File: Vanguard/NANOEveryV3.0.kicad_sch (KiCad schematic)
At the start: 57 parts, among them IC1 MPM3610, J1 -, J2 DNP, Q1 BSS138PS, Q2 BSS138PS, U1 ATMEGA4809, U2 AP2112K-3.3, U3 ATSAMD11D14A, U4 ICM-20602, U5 LM34DM_NOPB

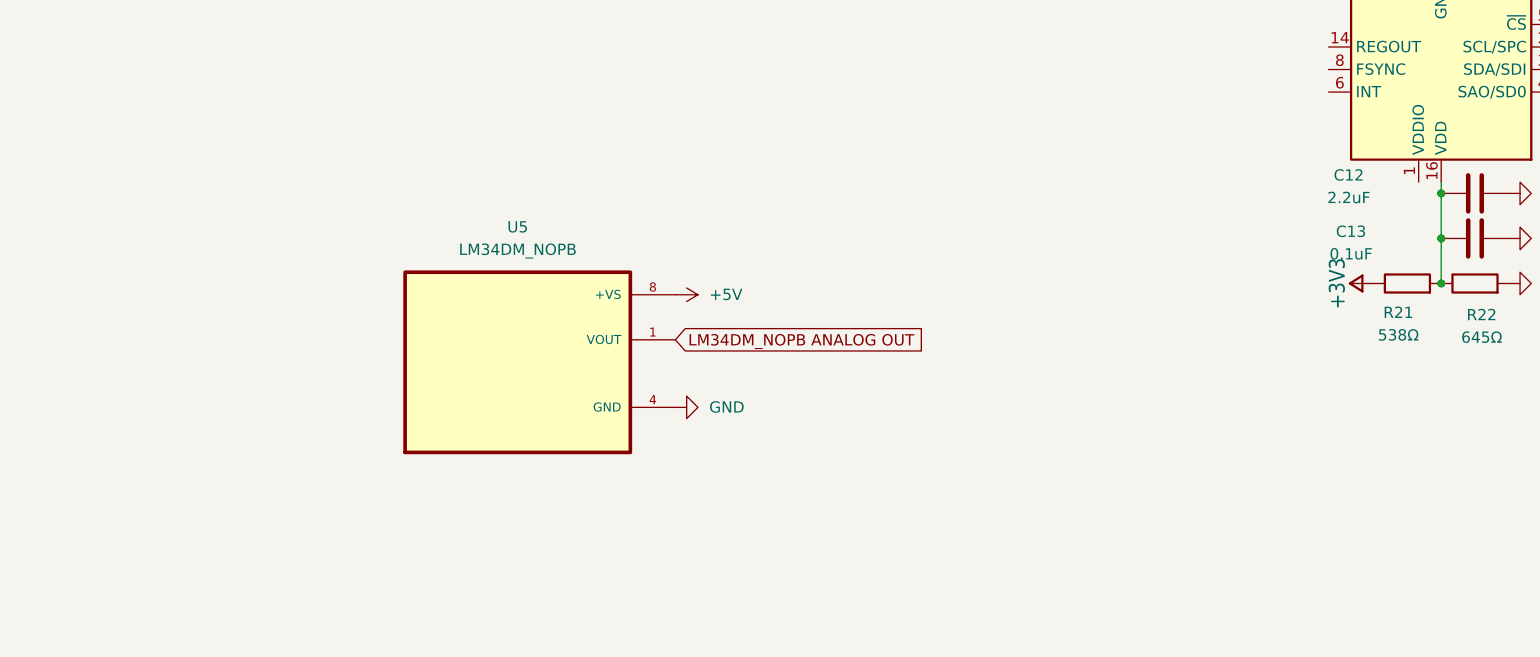
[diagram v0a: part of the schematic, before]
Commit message: Added 2 decoupling capacitors to the temp. sensor
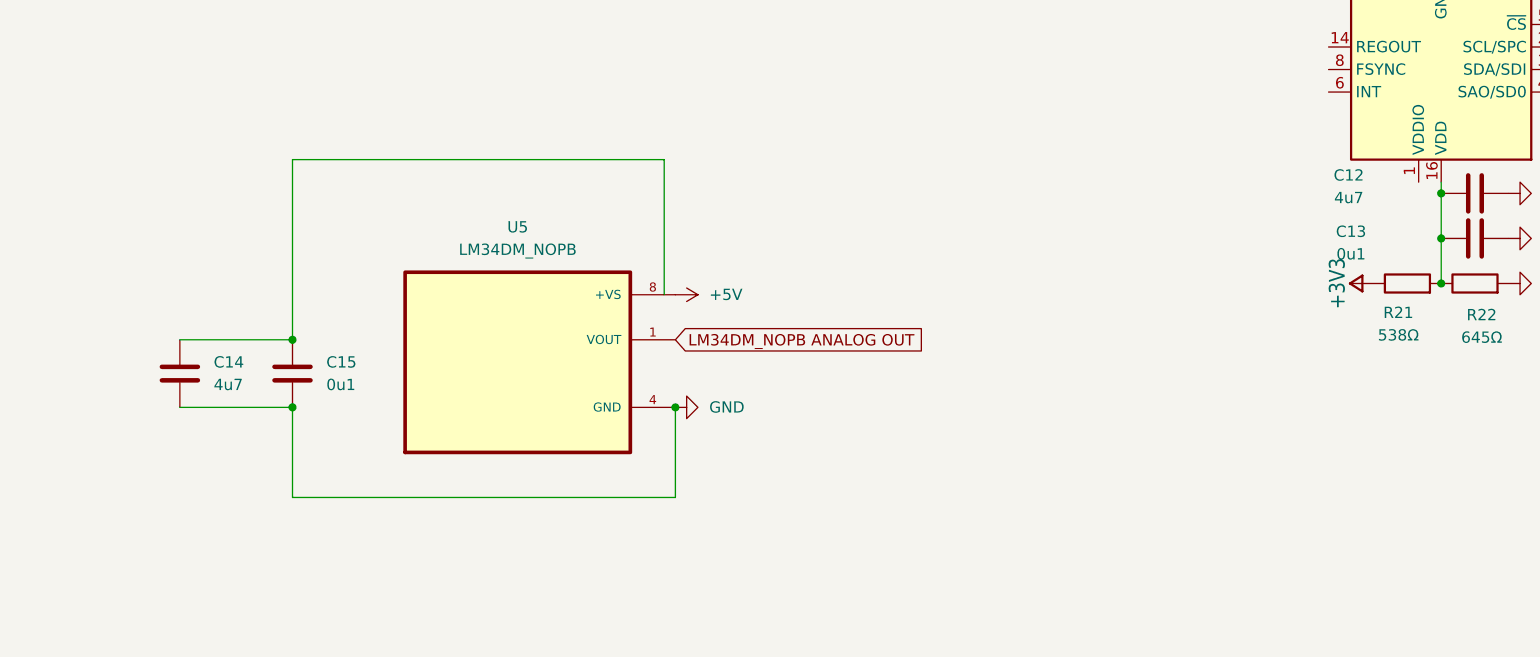
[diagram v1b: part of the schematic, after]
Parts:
- added C14: 4u7, symbol Device:C
- added C15: 0u1, symbol Device:C
- C12: value 2.2uF -> 4u7
- C13: value 0.1uF -> 0u1
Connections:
- net GND: now also C14.2, C15.2
- new net: C14.1, C15.1
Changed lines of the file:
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@@
 	)
 	(junction
+		(at 82.55 213.36)
+		(diameter 0)
+		(color 0 0 0 0)
+	)
+	(junction
 		(at 212.09 201.93)
 		(diameter 0)
@@
 	)
 	(junction
+		(at 125.73 220.98)
+		(diameter 0)
+		(color 0 0 0 0)
+	)
+	(junction
 		(at 59.69 152.4)
 		(diameter 0)
@@
 	)
 	(junction
+		(at 82.55 220.98)
+		(diameter 0)
+		(color 0 0 0 0)
+	)
+	(junction
 		(at 248.92 208.28)
 		(diameter 0)
@@
 	(wire
 		(pts
+			(xy 124.46 193.04) (xy 124.46 208.28)
+		)
+		(stroke
+			(width 0)
+			(type default)
+		)
+	)
+	(wire
+		(pts
 			(xy 375.92 186.69) (xy 353.06 186.69)
 		)
@@
 	(wire
 		(pts
+			(xy 125.73 220.98) (xy 125.73 231.14)
+		)
+		(stroke
+			(width 0)
+			(type default)
+		)
+	)
+	(wire
+		(pts
 			(xy 78.74 152.4) (xy 99.06 152.4)
 		)
@@
 	(wire
 		(pts
+			(xy 69.85 220.98) (xy 82.55 220.98)
+		)
+		(stroke
+			(width 0)
+			(type default)
+		)
+	)
+	(wire
+		(pts
 			(xy 149.86 33.02) (xy 149.86 36.83)
 		)
@@
 	(wire
 		(pts
+			(xy 82.55 231.14) (xy 125.73 231.14)
+		)
+		(stroke
+			(width 0)
+			(type default)
+		)
+	)
+	(wire
+		(pts
 			(xy 330.2 83.82) (xy 350.52 83.82)
 		)
@@
 	(wire
 		(pts
+			(xy 82.55 213.36) (xy 82.55 193.04)
+		)
+		(stroke
+			(width 0)
+			(type default)
+		)
+	)
+	(wire
+		(pts
 			(xy 184.15 123.19) (xy 186.69 123.19)
 		)
@@
 	(wire
 		(pts
+			(xy 82.55 220.98) (xy 82.55 231.14)
+		)
+		(stroke
+			(width 0)
+			(type default)
+		)
+	)
+	(wire
+		(pts
 			(xy 180.34 107.95) (xy 187.96 107.95)
 		)
@@
 	(wire
 		(pts
+			(xy 69.85 213.36) (xy 82.55 213.36)
+		)
+		(stroke
+			(width 0)
+			(type default)
+		)
+	)
+	(wire
+		(pts
 			(xy 63.5 152.4) (xy 59.69 152.4)
 		)
@@
 		)
 	)
+	(wire
+		(pts
+			(xy 82.55 193.04) (xy 124.46 193.04)
+		)
+		(stroke
+			(width 0)
+			(type default)
+		)
+	)
 	(bus
 		(pts
@@
 			)
 		)
-		(property "Value" "2.2uF"
+		(property "Value" "4u7"
 			(at 201.676 197.358 90)
 			(effects
@@
 	)
 	(symbol
+		(lib_id "Device:C")
+		(at 82.55 217.17 0)
+		(unit 1)
+		(exclude_from_sim no)
+		(in_bom yes)
+		(on_board yes)
+		(dnp no)
+		(fields_autoplaced yes)
+		(property "Reference" "C15"
+			(at 86.36 215.8999 0)
+			(effects
+				(font
+					(size 1.27 1.27)
+				)
+				(justify left)
+			)
+		)
+		(property "Value" "0u1"
+			(at 86.36 218.4399 0)
+			(effects
+				(font
+					(size 1.27 1.27)
+				)
+				(justify left)
+			)
+		)
+		(property "Footprint" ""
+			(at 83.5152 220.98 0)
+			(effects
+				(font
+					(size 1.27 1.27)
+				)
+				(hide yes)
+			)
+		)
+		(property "Datasheet" "~"
+			(at 82.55 217.17 0)
+			(effects
+				(font
+					(size 1.27 1.27)
+				)
+				(hide yes)
+			)
+		)
+		(property "Description" "Unpolarized capacitor"
+			(at 82.55 217.17 0)
+			(effects
+				(font
+					(size 1.27 1.27)
+				)
+				(hide yes)
+			)
+		)
+		(pin "2"
+		)
+		(pin "1"
+		)
+		(instances
+			(project ""
+				(path "/34ea8acc-c59c-4b5c-bba1-2d3f07551c63"
+					(reference "C15")
+					(unit 1)
+				)
+			)
+		)
+	)
+	(symbol
 		(lib_id "power:GND")
 		(at 219.71 196.85 90)
@@
 			)
 		)
-		(property "Value" "0.1uF"
+		(property "Value" "0u1"
 			(at 201.93 203.708 90)
 			(effects
@@
 					(unit 1)
 				)
+			)
+		)
+	)
+	(symbol
+		(lib_id "Device:C")
+		(at 69.85 217.17 0)
+		(unit 1)
+		(exclude_from_sim no)
+		(in_bom yes)
+		(on_board yes)
+		(dnp no)
+		(fields_autoplaced yes)
+		(property "Reference" "C14"
+			(at 73.66 215.8999 0)
+			(effects
+				(font
+					(size 1.27 1.27)
+				)
+				(justify left)
+			)
+		)
+		(property "Value" "4u7"
+			(at 73.66 218.4399 0)
+			(effects
+				(font
+					(size 1.27 1.27)
+				)
+				(justify left)
+			)
+		)
+		(property "Footprint" ""
+			(at 70.8152 220.98 0)
+			(effects
+				(font
+					(size 1.27 1.27)
+				)
+				(hide yes)
+			)
+		)
+		(property "Datasheet" "~"
+			(at 69.85 217.17 0)
+			(effects
+				(font
+					(size 1.27 1.27)
+				)
+				(hide yes)
+			)
+		)
+		(property "Description" "Unpolarized capacitor"
+			(at 69.85 217.17 0)
+			(effects
+				(font
+					(size 1.27 1.27)
+				)
+				(hide yes)
+			)
+		)
+		(pin "2"
+		)
+		(pin "1"
+		)
+		(instances
+			(project ""
+				(path "/34ea8acc-c59c-4b5c-bba1-2d3f07551c63"
+					(reference "C14")
+					(unit 1)
+				)

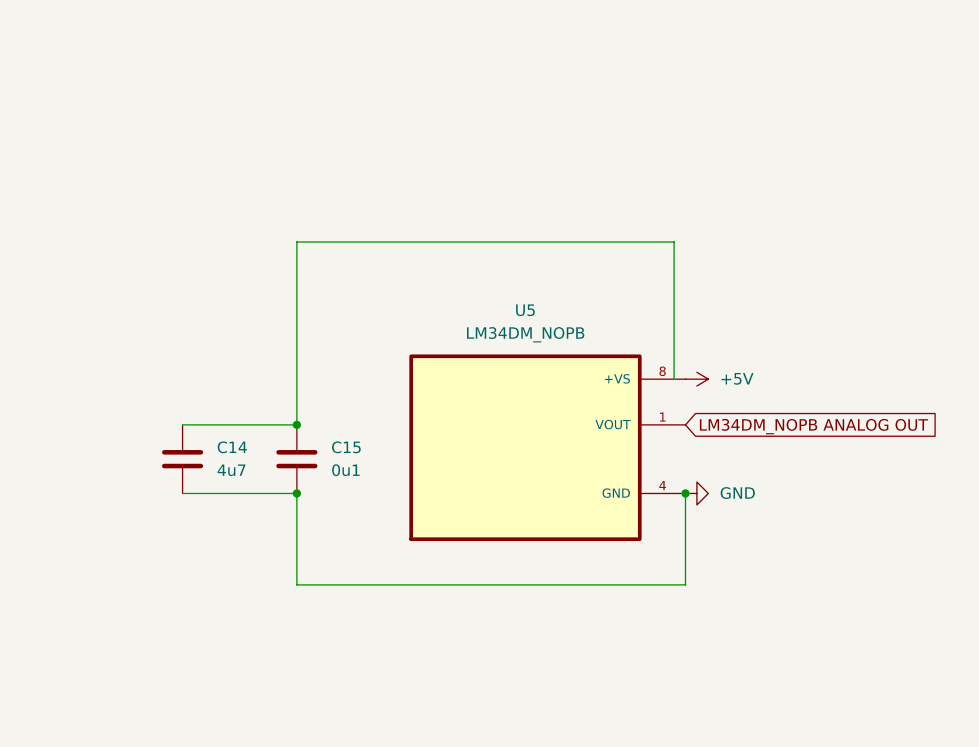
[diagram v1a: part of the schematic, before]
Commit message: slight changes in the capacitor arrangement
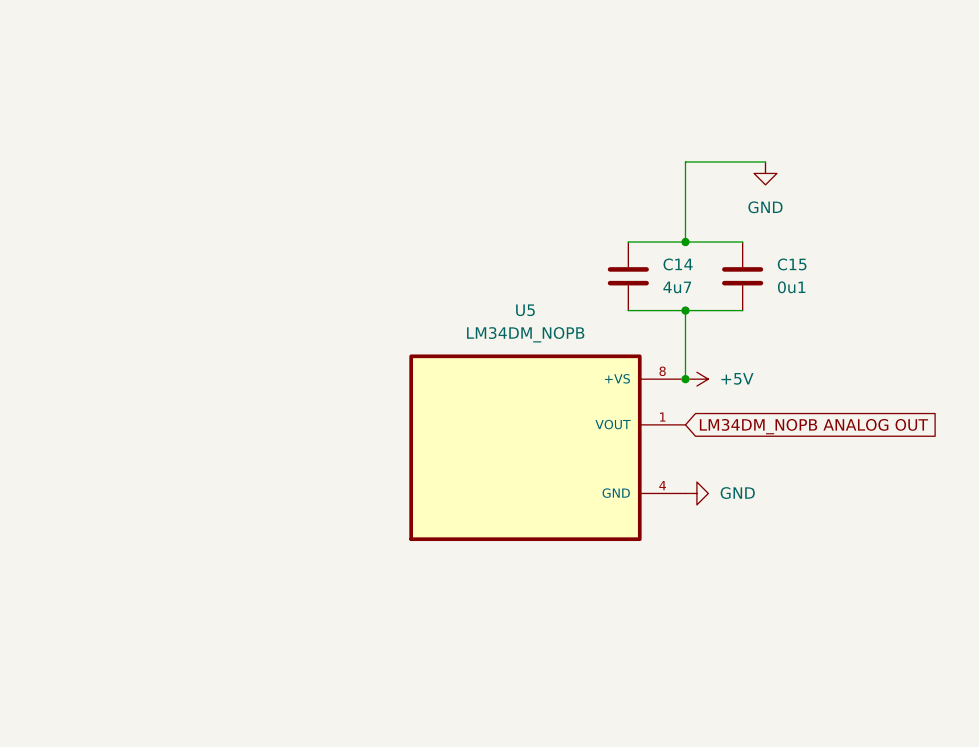
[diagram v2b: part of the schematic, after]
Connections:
- net +5V: now also C14.2, C15.2
- net GND: now also C14.1, C15.1; no longer C14.2, C15.2

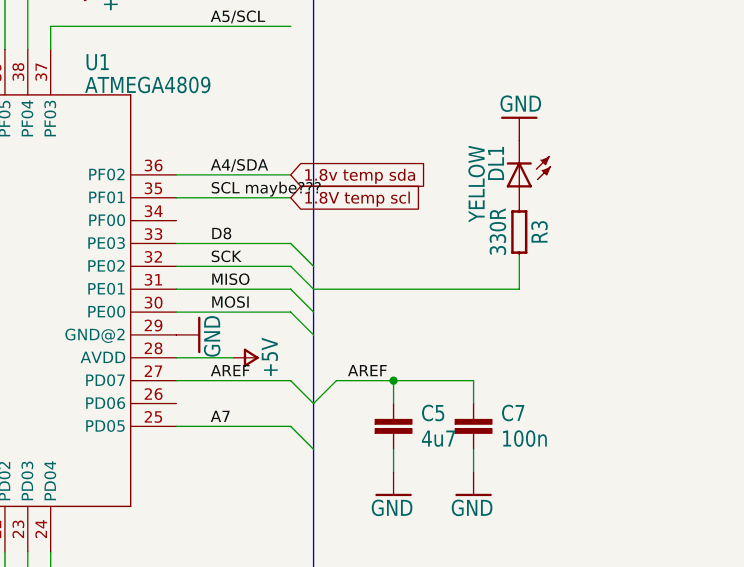
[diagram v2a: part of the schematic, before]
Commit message: finished layout except sd card
lots of discontinuities need to be fixed
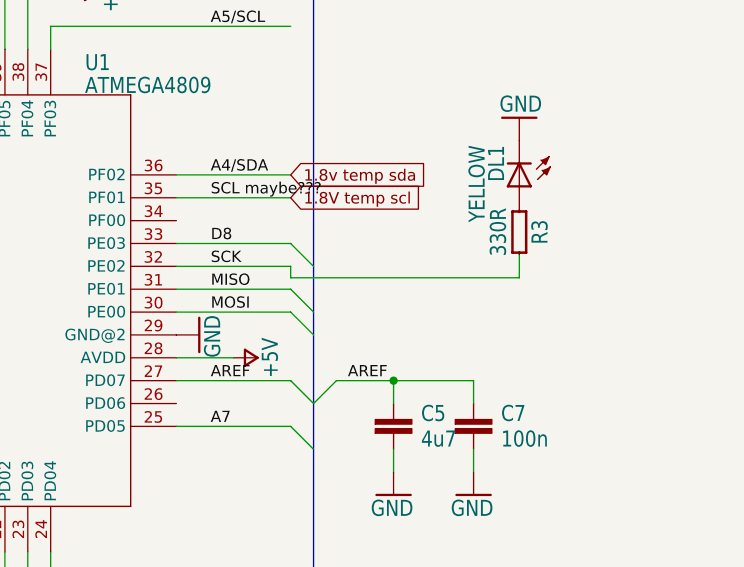
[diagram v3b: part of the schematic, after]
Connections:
- net SCK: now also R3.2
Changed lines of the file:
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@@
 	)
 	(bus_entry
-		(at 350.52 184.15)
-		(size 2.54 2.54)
-		(stroke
-			(width 0)
-			(type default)
-		)
-	)
-	(bus_entry
 		(at 350.52 88.9)
 		(size 2.54 2.54)
@@
 		)
 	)
-	(wire
-		(pts
-			(xy 375.92 186.69) (xy 353.06 186.69)
-		)
-		(stroke
-			(width 0)
-			(type default)
-		)
-	)
 	(bus
 		(pts
@@
 	(wire
 		(pts
+			(xy 350.52 184.15) (xy 350.52 185.42)
+		)
+		(stroke
+			(width 0.1524)
+			(type solid)
+		)
+	)
+	(wire
+		(pts
 			(xy 248.92 208.28) (xy 264.16 208.28)
 		)
@@
 	(wire
 		(pts
-			(xy 375.92 182.88) (xy 375.92 186.69)
+			(xy 375.92 182.88) (xy 375.92 185.42)
 		)
 		(stroke
@@
 	(bus
 		(pts
-			(xy 353.06 186.69) (xy 353.06 184.15)
+			(xy 353.06 184.15) (xy 353.06 189.23)
 		)
 		(stroke
@@
 	(wire
 		(pts
+			(xy 350.52 185.42) (xy 375.92 185.42)
+		)
+		(stroke
+			(width 0.1524)
+			(type solid)
+		)
+	)
+	(wire
+		(pts
 			(xy 87.63 50.8) (xy 90.17 50.8)
 		)
@@
 		)
 	)
-	(bus
-		(pts
-			(xy 353.06 189.23) (xy 353.06 186.69)
-		)
-		(stroke
-			(width 0.762)
-			(type solid)
-		)
-	)
 	(wire
 		(pts
@@
 	)
 	(symbol
+		(lib_id "NANOEveryV3.0-eagle-import:+3V3")
+		(at 149.86 27.94 0)
+		(unit 1)
+		(exclude_from_sim no)
+		(in_bom yes)
+		(on_board yes)
+		(dnp no)
+		(property "Reference" "#+3V04"
+			(at 149.86 27.94 0)
+			(effects
+				(font
+					(size 1.27 1.27)
+				)
+				(hide yes)
+			)
+		)
+		(property "Value" "+3V3"
+			(at 149.86 27.432 0)
+			(effects
+				(font
+					(size 1.778 1.5113)
+				)
+				(justify bottom)
+			)
+		)
+		(property "Footprint" ""
+			(at 149.86 27.94 0)
+			(effects
+				(font
+					(size 1.27 1.27)
+				)
+				(hide yes)
+			)
+		)
+		(property "Datasheet" ""
+			(at 149.86 27.94 0)
+			(effects
+				(font
+					(size 1.27 1.27)
+				)
+				(hide yes)
+			)
+		)
+		(property "Description" ""
+			(at 149.86 27.94 0)
+			(effects
+				(font
+					(size 1.27 1.27)
+				)
+				(hide yes)
+			)
+		)
+		(pin "1"
+		)
+		(instances
+			(project "NANOEveryV3.0"
+				(path "/34ea8acc-c59c-4b5c-bba1-2d3f07551c63"
+					(reference "#+3V04")
+					(unit 1)
+				)
+			)
+		)
+	)
+	(symbol
 		(lib_id "NANOEveryV3.0-eagle-import:R-0402")
 		(at 187.96 97.79 90)
@@
 					(unit 1)
 				)
-			)
-		)
-	)
-	(symbol
-		(lib_id "NANOEveryV3.0-eagle-import:+3V3")
-		(at 149.86 27.94 0)
-		(unit 1)
-		(exclude_from_sim no)
-		(in_bom yes)
-		(on_board yes)
-		(dnp no)
-		(property "Reference" "#+3V04"
-			(at 149.86 27.94 0)
-			(effects
-				(font
-					(size 1.27 1.27)
-				)
-				(hide yes)
-			)
-		)
-		(property "Value" "+3V3"
-			(at 149.86 27.432 0)
-			(effects
-				(font
-					(size 1.778 1.5113)
-				)
-				(justify bottom)
-			)
-		)
-		(property "Footprint" ""
-			(at 149.86 27.94 0)
-			(effects
-				(font
-					(size 1.27 1.27)
-				)
-				(hide yes)
-			)
-		)
-		(property "Datasheet" ""
-			(at 149.86 27.94 0)
-			(effects
-				(font
-					(size 1.27 1.27)
-				)
-				(hide yes)
-			)
-		)
-		(property "Description" ""
-			(at 149.86 27.94 0)
-			(effects
-				(font
-					(size 1.27 1.27)
-				)
-				(hide yes)
-			)
-		)
-		(pin "1"
-		)
-		(instances
-			(project ""
-				(path "/34ea8acc-c59c-4b5c-bba1-2d3f07551c63"
-					(reference "#+3V04")
-					(unit 1)
-				)

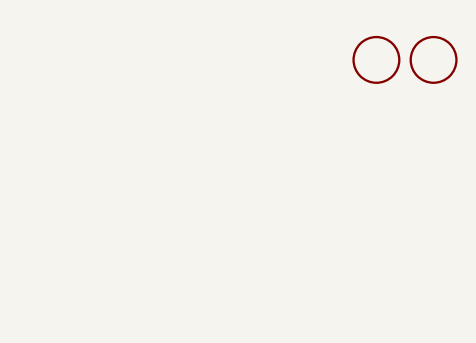
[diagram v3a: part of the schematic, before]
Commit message: added 2 footprints
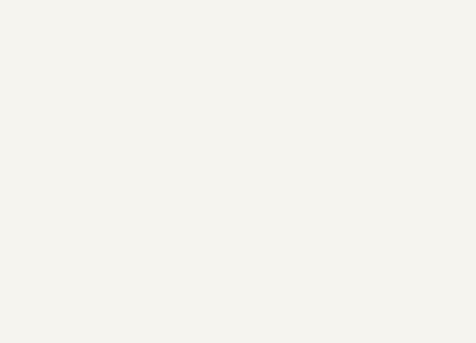
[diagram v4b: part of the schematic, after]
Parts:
- removed FD1, FD2: DNP, TestPoint:TestPoint_THTPad_1.0x1.0mm_Drill0.5mm, symbol NANOEveryV3.0-eagle-import:FIDUCIAL-1.5MM
- C14, C15: footprint (none) -> Capacitor_SMD:C_0402_1005Metric
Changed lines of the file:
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@@
 	)
 	(symbol
-		(lib_id "NANOEveryV3.0-eagle-import:FIDUCIAL-1.5MM")
-		(at 396.24 27.94 0)
-		(unit 1)
-		(exclude_from_sim no)
-		(in_bom yes)
-		(on_board yes)
-		(dnp no)
-		(property "Reference" "FD2"
-			(at 396.24 27.94 0)
-			(effects
-				(font
-					(size 1.27 1.27)
-				)
-				(hide yes)
-			)
-		)
-		(property "Value" "DNP"
-			(at 396.24 27.94 0)
-			(effects
-				(font
-					(size 1.27 1.27)
-				)
-				(hide yes)
-			)
-		)
-		(property "Footprint" "TestPoint:TestPoint_THTPad_1.0x1.0mm_Drill0.5mm"
-			(at 396.24 27.94 0)
-			(effects
-				(font
-					(size 1.27 1.27)
-				)
-				(hide yes)
-			)
-		)
-		(property "Datasheet" ""
-			(at 396.24 27.94 0)
-			(effects
-				(font
-					(size 1.27 1.27)
-				)
-				(hide yes)
-			)
-		)
-		(property "Description" ""
-			(at 396.24 27.94 0)
-			(effects
-				(font
-					(size 1.27 1.27)
-				)
-				(hide yes)
-			)
-		)
-		(instances
-			(project ""
-				(path "/34ea8acc-c59c-4b5c-bba1-2d3f07551c63"
-					(reference "FD2")
-					(unit 1)
-				)
-			)
-		)
-	)
-	(symbol
 		(lib_id "NANOEveryV3.0-eagle-import:+5V")
 		(at 328.93 153.67 270)
@@
 	)
 	(symbol
-		(lib_id "NANOEveryV3.0-eagle-import:FIDUCIAL-1.5MM")
-		(at 389.89 27.94 0)
-		(unit 1)
-		(exclude_from_sim no)
-		(in_bom yes)
-		(on_board yes)
-		(dnp no)
-		(property "Reference" "FD1"
-			(at 389.89 27.94 0)
-			(effects
-				(font
-					(size 1.27 1.27)
-				)
-				(hide yes)
-			)
-		)
-		(property "Value" "DNP"
-			(at 389.89 27.94 0)
-			(effects
-				(font
-					(size 1.27 1.27)
-				)
-				(hide yes)
-			)
-		)
-		(property "Footprint" "TestPoint:TestPoint_THTPad_1.0x1.0mm_Drill0.5mm"
-			(at 389.89 27.94 0)
-			(effects
-				(font
-					(size 1.27 1.27)
-				)
-				(hide yes)
-			)
-		)
-		(property "Datasheet" ""
-			(at 389.89 27.94 0)
-			(effects
-				(font
-					(size 1.27 1.27)
-				)
-				(hide yes)
-			)
-		)
-		(property "Description" ""
-			(at 389.89 27.94 0)
-			(effects
-				(font
-					(size 1.27 1.27)
-				)
-				(hide yes)
-			)
-		)
-		(instances
-			(project ""
-				(path "/34ea8acc-c59c-4b5c-bba1-2d3f07551c63"
-					(reference "FD1")
-					(unit 1)
-				)
-			)
-		)
-	)
-	(symbol
 		(lib_id "NANOEveryV3.0-eagle-import:R-0402")
 		(at 212.09 146.05 90)
@@
 			)
 		)
-		(property "Footprint" ""
+		(property "Footprint" "Capacitor_SMD:C_0402_1005Metric"
 			(at 133.0452 200.66 0)
 			(effects
@@
 			)
 		)
-		(property "Footprint" ""
+		(property "Footprint" "Capacitor_SMD:C_0402_1005Metric"
 			(at 120.3452 200.66 0)
 			(effects
